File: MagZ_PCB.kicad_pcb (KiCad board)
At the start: 4 copper layers, 42 x 42 mm, 11 parts, among them J6 MTQZ, J8 PQ9-Connector

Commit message: Oops...forgot to save
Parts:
- added G***: LOGO, POQUITO_Panel_Library:POQUITO-7mm, F.Cu at (193.2, 87.2)
- added G***: LOGO, POQUITO_Panel_Library:WSOF-5, F.Cu at (194.6, 70.2)
- added G***: LOGO, POQUITO_Panel_Library:POQUITO-29mm, B.Cu at (193.0, 70.0)
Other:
- board text added: "Designed by Niki Sajjad"
- board text added: "MTQ Z board v1"

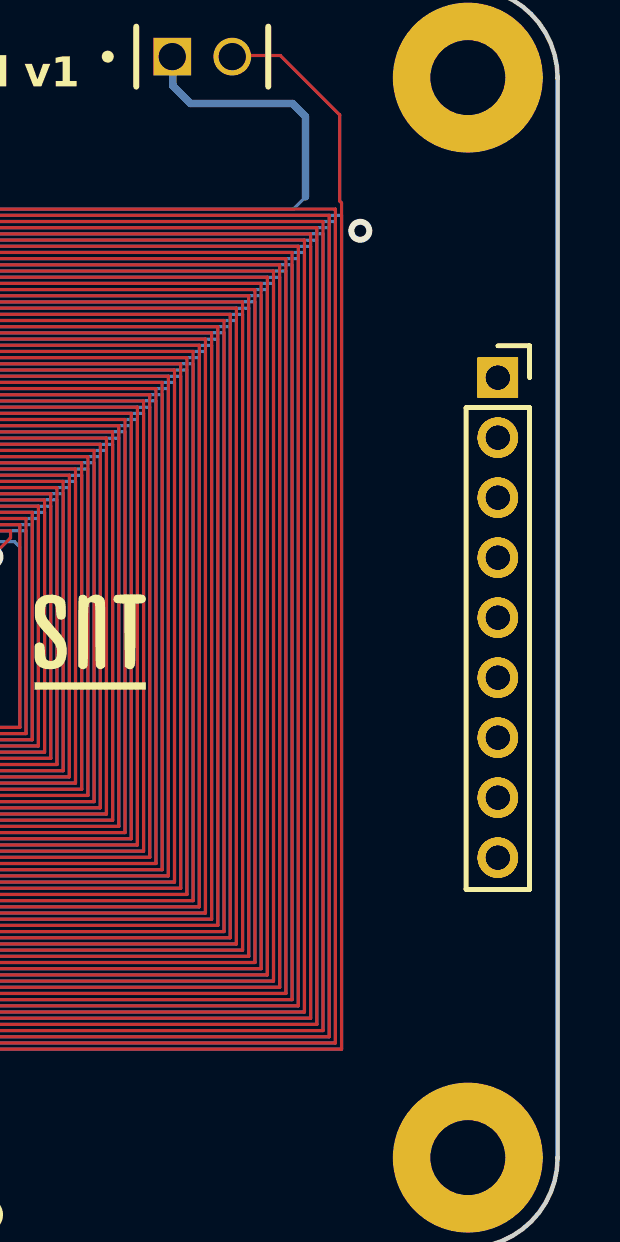
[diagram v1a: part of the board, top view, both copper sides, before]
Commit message: Use pogo pins; move diode to back
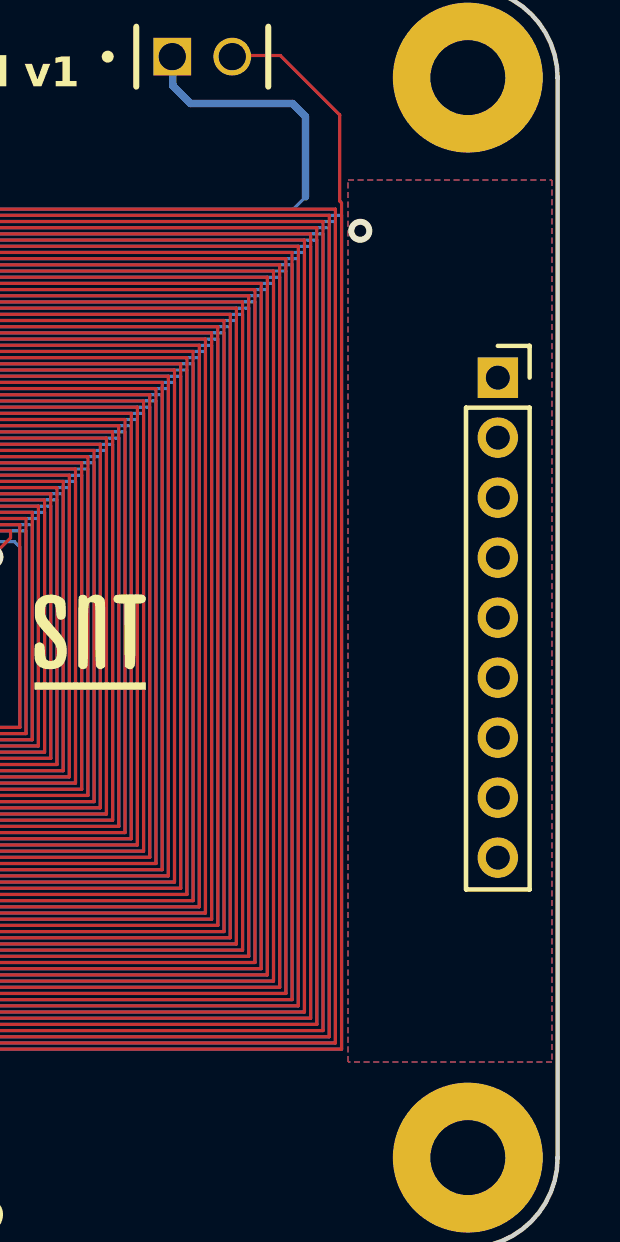
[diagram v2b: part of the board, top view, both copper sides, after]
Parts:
- removed PQ9: PQ9-Connector, Connector_PinSocket_2.00mm:PinSocket_1x09_P2.00mm_Vertical
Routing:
- added copper zone on B.Cu, net GND
- added copper zone on F.Cu, net GND
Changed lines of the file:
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@@
 (kicad_pcb (version 20221018) (generator pcbnew)
   (general
-    (thickness 1.6)
+    (thickness 0.895)
   )
   (paper "A4")
@@
   (net 7 "unconnected-(J8-V3-Pad7)")
   (net 8 "+5V")
-  (net 9 "Net-(PQ9-Pad8)")
-  (net 10 "Net-(PQ9-Pad7)")
-  (net 11 "Net-(PQ9-Pad6)")
-  (net 12 "Net-(PQ9-Pad5)")
-  (net 13 "Net-(PQ9-Pad4)")
-  (net 14 "Net-(PQ9-Pad3)")
-  (net 15 "Net-(PQ9-Pad2)")
-  (net 16 "Net-(PQ9-Pad1)")
   (footprint "Connector_PinSocket_2.00mm:PinSocket_1x09_P2.00mm_Vertical" (layer "F.Cu")
     (at 213.194 61.5879)
@@
       (stroke (width 0) (type solid)) (fill solid) (layer "F.SilkS"))
   )
-  (footprint "Connector_PinSocket_2.00mm:PinSocket_1x09_P2.00mm_Vertical" locked (layer "F.Cu")
-    (at 213.194 61.5879)
-    (descr "Through hole straight socket strip, 1x09, 2.00mm pitch, single row (from Kicad 4.0.7), script generated")
-    (tags "Through hole socket strip THT 1x09 2.00mm single row")
-    (attr through_hole)
-    (fp_text reference "PQ9" (at 0 -2.5 unlocked) (layer "F.SilkS") hide
-        (effects (font (size 0.5 0.5) (thickness 0.1)))
-    )
-    (fp_text value "PQ9-Connector" (at 0 18.5 unlocked) (layer "F.Fab") hide
-        (effects (font (size 0.5 0.5) (thickness 0.1)))
-    )
-    (fp_text user "${REFERENCE}" (at 0 8 90 unlocked) (layer "F.Fab") hide
-        (effects (font (size 0.5 0.5) (thickness 0.1)))
-    )
-    (fp_line (start -1.06 1) (end -1.06 17.06)
-      (stroke (width 0.15) (type solid)) (layer "F.SilkS"))
-    (fp_line (start -1.06 1) (end 1.06 1)
-      (stroke (width 0.15) (type solid)) (layer "F.SilkS"))
-    (fp_line (start -1.06 17.06) (end 1.06 17.06)
-      (stroke (width 0.15) (type solid)) (layer "F.SilkS"))
-    (fp_line (start 0 -1.06) (end 1.06 -1.06)
-      (stroke (width 0.15) (type solid)) (layer "F.SilkS"))
-    (fp_line (start 1.06 -1.06) (end 1.06 0)
-      (stroke (width 0.15) (type solid)) (layer "F.SilkS"))
-    (fp_line (start 1.06 1) (end 1.06 17.06)
-      (stroke (width 0.15) (type solid)) (layer "F.SilkS"))
-    (fp_line (start -1.5 -1.5) (end 1.5 -1.5)
-      (stroke (width 0.05) (type solid)) (layer "F.CrtYd"))
-    (fp_line (start -1.5 17.5) (end -1.5 -1.5)
-      (stroke (width 0.05) (type solid)) (layer "F.CrtYd"))
-    (fp_line (start 1.5 -1.5) (end 1.5 17.5)
-      (stroke (width 0.05) (type solid)) (layer "F.CrtYd"))
-    (fp_line (start 1.5 17.5) (end -1.5 17.5)
-      (stroke (width 0.05) (type solid)) (layer "F.CrtYd"))
-    (fp_line (start -1 -1) (end 0.5 -1)
-      (stroke (width 0.1) (type solid)) (layer "F.Fab"))
-    (fp_line (start -1 17) (end -1 -1)
-      (stroke (width 0.1) (type solid)) (layer "F.Fab"))
-    (fp_line (start 0.5 -1) (end 1 -0.5)
-      (stroke (width 0.1) (type solid)) (layer "F.Fab"))
-    (fp_line (start 1 -0.5) (end 1 17)
-      (stroke (width 0.1) (type solid)) (layer "F.Fab"))
-    (fp_line (start 1 17) (end -1 17)
-      (stroke (width 0.1) (type solid)) (layer "F.Fab"))
-    (pad "1" thru_hole rect locked (at 0 0) (size 1.35 1.35) (drill 0.8) (layers "*.Cu" "*.Mask")
-      (net 16 "Net-(PQ9-Pad1)"))
-    (pad "2" thru_hole oval locked (at 0 2) (size 1.35 1.35) (drill 0.8) (layers "*.Cu" "*.Mask")
-      (net 15 "Net-(PQ9-Pad2)"))
-    (pad "3" thru_hole oval locked (at 0 4) (size 1.35 1.35) (drill 0.8) (layers "*.Cu" "*.Mask")
-      (net 14 "Net-(PQ9-Pad3)"))
-    (pad "4" thru_hole oval locked (at 0 6) (size 1.35 1.35) (drill 0.8) (layers "*.Cu" "*.Mask")
-      (net 13 "Net-(PQ9-Pad4)"))
-    (pad "5" thru_hole oval locked (at 0 8) (size 1.35 1.35) (drill 0.8) (layers "*.Cu" "*.Mask")
-      (net 12 "Net-(PQ9-Pad5)"))
-    (pad "6" thru_hole oval locked (at 0 10) (size 1.35 1.35) (drill 0.8) (layers "*.Cu" "*.Mask")
-      (net 11 "Net-(PQ9-Pad6)"))
-    (pad "7" thru_hole oval locked (at 0 12) (size 1.35 1.35) (drill 0.8) (layers "*.Cu" "*.Mask")
-      (net 10 "Net-(PQ9-Pad7)"))
-    (pad "8" thru_hole oval locked (at 0 14) (size 1.35 1.35) (drill 0.8) (layers "*.Cu" "*.Mask")
-      (net 9 "Net-(PQ9-Pad8)"))
-    (pad "9" thru_hole oval locked (at 0 16) (size 1.35 1.35) (drill 0.8) (layers "*.Cu" "*.Mask")
-      (net 13 "Net-(PQ9-Pad4)"))
-    (model "${KISYS3DMOD}/Connector_PinSocket_2.00mm.3dshapes/PinSocket_1x09_P2.00mm_Vertical.wrl"
-      (offset (xyz 0 0 0))
-      (scale (xyz 1 1 1))
-      (rotate (xyz 0 0 0))
-    )
-  )
   (footprint "MountingHole:MountingHole_2.5mm_Pad" locked (layer "F.Cu")
     (at 176.194 51.5879)
@@
   (segment (start 183.6981 59.6835) (end 183.6981 80.2587) (width 0.1062) (layer "B.Cu") (net 0))
   (segment (start 184.5231 60.5085) (end 184.5231 79.4337) (width 0.1062) (layer "B.Cu") (net 0))
+  (zone (net 1) (net_name "GND") (layer "F.Cu") (hatch edge 0.5)
+    (connect_pads (clearance 0.5))
+    (min_thickness 0.25) (filled_areas_thickness no)
+    (fill yes (thermal_gap 0.5) (thermal_bridge_width 0.5))
+    (polygon
+      (pts
+        (xy 215 55)
+        (xy 215 84.4)
+        (xy 208.2 84.4)
+        (xy 208.2 55)
+      )
+    )
+  )
+  (zone (net 1) (net_name "GND") (layer "B.Cu") (hatch edge 0.5)
+    (connect_pads (clearance 0.5))
+    (min_thickness 0.25) (filled_areas_thickness no)
+    (fill yes (thermal_gap 0.5) (thermal_bridge_width 0.5))
+    (polygon
+      (pts
+        (xy 215 55)
+        (xy 215 84.4)
+        (xy 208.2 84.4)
+        (xy 208.2 55)
+      )
+    )
+  )
 )

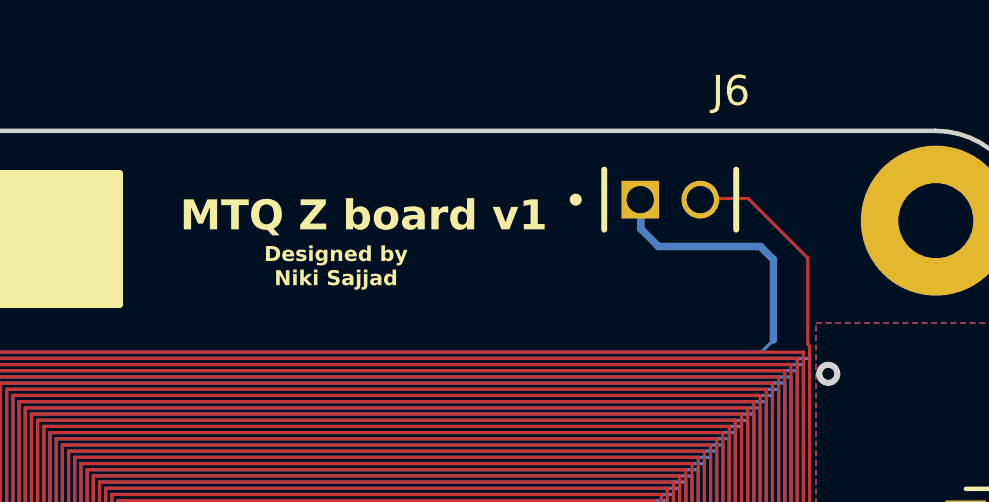
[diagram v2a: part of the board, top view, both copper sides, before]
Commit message: Flip misaligned pogo pins
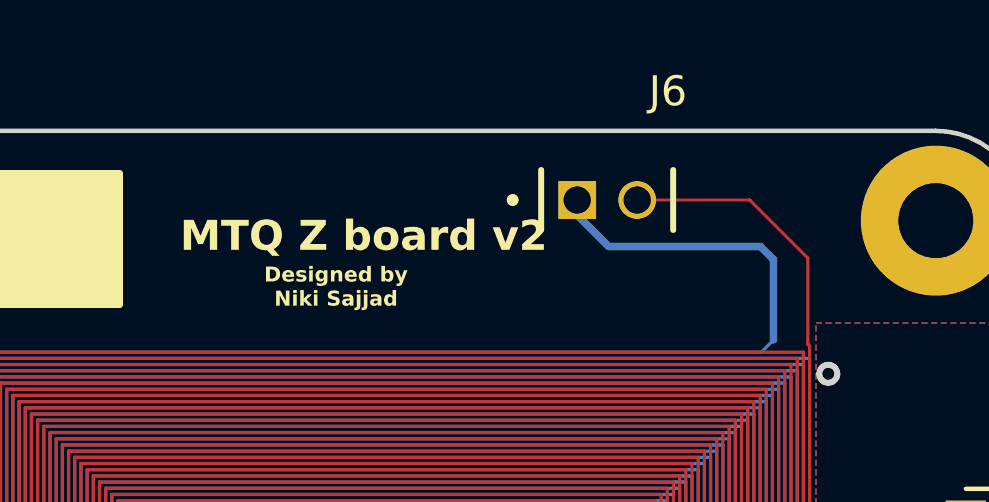
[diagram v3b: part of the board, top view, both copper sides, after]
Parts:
- moved J6 2.10 mm to (200.2, 50.9)
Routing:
- net (no net): track 14674.0 -> 14677.9 mm
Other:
- board text added: "MTQ Z board v2"
- board text removed: "MTQ Z board v1"

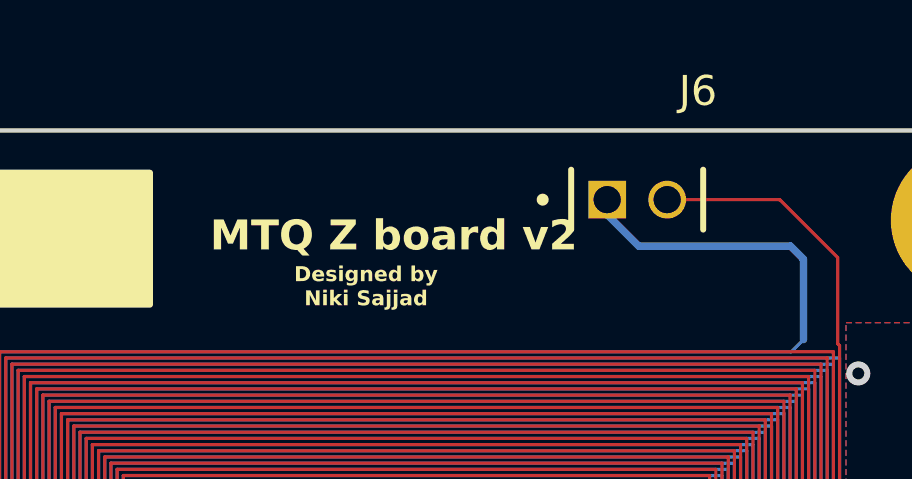
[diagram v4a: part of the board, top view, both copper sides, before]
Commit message: Fix PTH mounting holes for MTQ
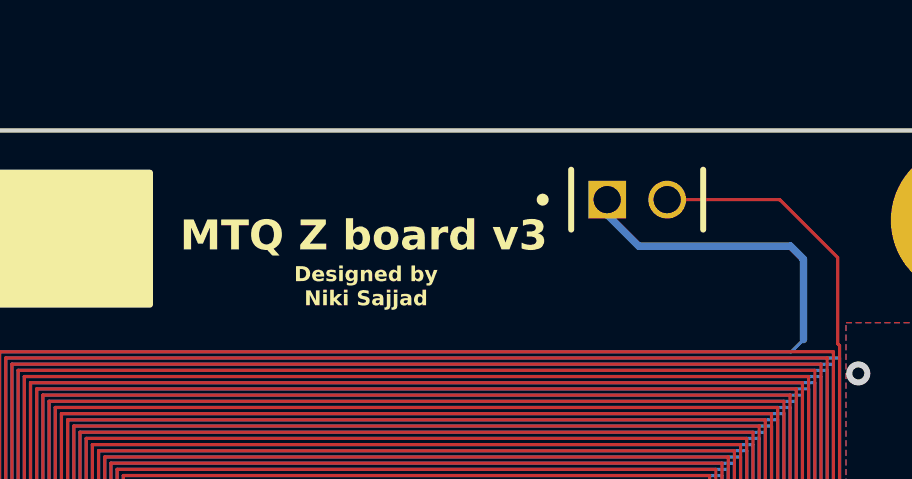
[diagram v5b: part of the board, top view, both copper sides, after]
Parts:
- removed REF** (x4): MountingHole_2.5mm_Pad, MountingHole:MountingHole_2.5mm_Pad
- added ?: , , F.Cu at (212.2, 87.6)
- added ?: , , F.Cu at (212.2, 51.6)
- added ?: , , F.Cu at (176.2, 87.6)
- added ?: , , F.Cu at (176.2, 51.6)
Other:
- board text added: "MTQ Z board v3"
- board text removed: "MTQ Z board v2"
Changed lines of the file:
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@@
       (solder_mask_margin 0.5) (clearance 0.5))
   )
+  (footprint "" (layer "F.Cu")
+    (at 212.194 87.5879)
+    (fp_text reference "" (at 0 0) (layer "F.SilkS")
+        (effects (font (size 1.27 1.27) (thickness 0.15)))
+    )
+    (fp_text value "" (at 0 0) (layer "F.SilkS")
+        (effects (font (size 1.27 1.27) (thickness 0.15)))
+    )
+    (pad "1" thru_hole circle (at 0 0) (size 5 5) (drill 2.5) (layers "*.Cu" "*.Mask")
+      (pinfunction "1") (pintype "input+no_connect"))
+  )
   (footprint "Fiducial:Fiducial_0.5mm_Mask1.5mm" (layer "F.Cu")
     (at 98.2428 120.958)
@@
     (property "SnapEDA_Link" "https://www.snapeda.com/parts/SQT-102-03-F-S/Samtec/view-part/?ref=snap")
     (attr through_hole)
-    (fp_text reference "J6" (at 3.025 -3.62) (layer "F.SilkS")
+    (fp_text reference "J6" (at 3.025 -3.62) (layer "F.SilkS") hide
         (effects (font (size 1 1) (thickness 0.15)))
     )
@@
       (pinfunction "02") (pintype "passive") (solder_mask_margin 0.102))
   )
+  (footprint "" (layer "F.Cu")
+    (at 212.194 51.5879)
+    (fp_text reference "" (at 0 0) (layer "F.SilkS")
+        (effects (font (size 1.27 1.27) (thickness 0.15)))
+    )
+    (fp_text value "" (at 0 0) (layer "F.SilkS")
+        (effects (font (size 1.27 1.27) (thickness 0.15)))
+    )
+    (pad "1" thru_hole circle (at 0 0) (size 5 5) (drill 2.5) (layers "*.Cu" "*.Mask")
+      (pinfunction "1") (pintype "input+no_connect"))
+  )
   (footprint "POQUITO_Panel_Library:POQUITO-7mm" (layer "F.Cu")
     (at 193.2 87.2)
@@
       (stroke (width 0) (type solid)) (fill solid) (layer "F.SilkS"))
   )
-  (footprint "MountingHole:MountingHole_2.5mm_Pad" locked (layer "F.Cu")
-    (at 176.194 51.5879)
-    (descr "Mounting Hole 2.5mm")
-    (tags "mounting hole 2.5mm")
-    (zone_connect 0)
-    (attr exclude_from_pos_files exclude_from_bom)
-    (fp_text reference "REF**" (at 0 -3.5 unlocked) (layer "F.SilkS") hide
-        (effects (font (size 0.5 0.5) (thickness 0.1)))
-    )
-    (fp_text value "MountingHole_2.5mm_Pad" (at -13 0 unlocked) (layer "F.Fab") hide
-        (effects (font (size 0.5 0.5) (thickness 0.1)))
-    )
-    (fp_text user "${REFERENCE}" (at 0.3 0 unlocked) (layer "F.Fab")
-        (effects (font (size 0.5 0.5) (thickness 0.1)))
-    )
-    (fp_circle (center 0 0) (end 2.5 0)
-      (stroke (width 0.15) (type solid)) (fill none) (layer "Cmts.User"))
-    (fp_circle (center 0 0) (end 2.75 0)
-      (stroke (width 0.05) (type solid)) (fill none) (layer "F.CrtYd"))
-    (pad "" np_thru_hole circle locked (at 0 0) (size 5 5) (drill 2.5) (layers "*.Cu" "*.Mask")
-      (zone_connect 0))
-  )
-  (footprint "MountingHole:MountingHole_2.5mm_Pad" locked (layer "F.Cu")
-    (at 176.194 87.5879)
-    (descr "Mounting Hole 2.5mm")
-    (tags "mounting hole 2.5mm")
-    (attr exclude_from_pos_files exclude_from_bom)
-    (fp_text reference "REF**" (at 0 -3.5 unlocked) (layer "F.SilkS") hide
-        (effects (font (size 0.5 0.5) (thickness 0.1)))
-    )
-    (fp_text value "MountingHole_2.5mm_Pad" (at -13 0 unlocked) (layer "F.Fab") hide
-        (effects (font (size 0.5 0.5) (thickness 0.1)))
-    )
-    (fp_text user "${REFERENCE}" (at 0.3 0 unlocked) (layer "F.Fab")
-        (effects (font (size 0.5 0.5) (thickness 0.1)))
-    )
-    (fp_circle (center 0 0) (end 2.5 0)
-      (stroke (width 0.15) (type solid)) (fill none) (layer "Cmts.User"))
-    (fp_circle (center 0 0) (end 2.75 0)
-      (stroke (width 0.05) (type solid)) (fill none) (layer "F.CrtYd"))
-    (pad "" np_thru_hole circle locked (at 0 0) (size 5 5) (drill 2.5) (layers "*.Cu" "*.Mask"))
-  )
-  (footprint "MountingHole:MountingHole_2.5mm_Pad" locked (layer "F.Cu")
-    (at 212.194 87.5879)
-    (descr "Mounting Hole 2.5mm")
-    (tags "mounting hole 2.5mm")
-    (attr exclude_from_pos_files exclude_from_bom)
-    (fp_text reference "REF**" (at 0 -3.5 unlocked) (layer "F.SilkS") hide
-        (effects (font (size 0.5 0.5) (thickness 0.1)))
-    )
-    (fp_text value "MountingHole_2.5mm_Pad" (at 13 0 unlocked) (layer "F.Fab") hide
-        (effects (font (size 0.5 0.5) (thickness 0.1)))
-    )
-    (fp_text user "${REFERENCE}" (at 0.3 0 unlocked) (layer "F.Fab")
-        (effects (font (size 0.5 0.5) (thickness 0.1)))
-    )
-    (fp_circle (center 0 0) (end 2.5 0)
-      (stroke (width 0.15) (type solid)) (fill none) (layer "Cmts.User"))
-    (fp_circle (center 0 0) (end 2.75 0)
-      (stroke (width 0.05) (type solid)) (fill none) (layer "F.CrtYd"))
-    (pad "" np_thru_hole circle locked (at 0 0) (size 5 5) (drill 2.5) (layers "*.Cu" "*.Mask"))
-  )
   (footprint "POQUITO_Panel_Library:WSOF-5" (layer "F.Cu")
     (at 194.570376 70.225606)
@@
       (stroke (width 0) (type solid)) (fill solid) (layer "F.SilkS"))
   )
-  (footprint "MountingHole:MountingHole_2.5mm_Pad" locked (layer "F.Cu")
-    (at 212.194 51.5879)
-    (descr "Mounting Hole 2.5mm")
-    (tags "mounting hole 2.5mm")
-    (attr exclude_from_pos_files exclude_from_bom)
-    (fp_text reference "REF**" (at 0 -3.5 unlocked) (layer "F.SilkS") hide
-        (effects (font (size 0.5 0.5) (thickness 0.1)))
+  (footprint "" (layer "F.Cu")
+    (at 176.194 87.5879)
+    (fp_text reference "" (at 0 0) (layer "F.SilkS")
+        (effects (font (size 1.27 1.27) (thickness 0.15)))
     )
-    (fp_text value "MountingHole_2.5mm_Pad" (at 13 0 unlocked) (layer "F.Fab") hide
-        (effects (font (size 0.5 0.5) (thickness 0.1)))
+    (fp_text value "" (at 0 0) (layer "F.SilkS")
+        (effects (font (size 1.27 1.27) (thickness 0.15)))
     )
-    (fp_text user "${REFERENCE}" (at 0.3 0 unlocked) (layer "F.Fab")
-        (effects (font (size 0.5 0.5) (thickness 0.1)))
+    (pad "1" thru_hole circle (at 0 0) (size 5 5) (drill 2.5) (layers "*.Cu" "*.Mask")
+      (pinfunction "1") (pintype "input+no_connect"))
+  )
+  (footprint "" (layer "F.Cu")
+    (at 176.194 51.5879)
+    (fp_text reference "" (at 0 0) (layer "F.SilkS")
+        (effects (font (size 1.27 1.27) (thickness 0.15)))
     )
-    (fp_circle (center 0 0) (end 2.5 0)
-      (stroke (width 0.15) (type solid)) (fill none) (layer "Cmts.User"))
-    (fp_circle (center 0 0) (end 2.75 0)
-      (stroke (width 0.05) (type solid)) (fill none) (layer "F.CrtYd"))
-    (pad "" np_thru_hole circle locked (at 0 0) (size 5 5) (drill 2.5) (layers "*.Cu" "*.Mask"))
+    (fp_text value "" (at 0 0) (layer "F.SilkS")
+        (effects (font (size 1.27 1.27) (thickness 0.15)))
+    )
+    (pad "1" thru_hole circle (at 0 0) (size 5 5) (drill 2.5) (layers "*.Cu" "*.Mask")
+      (pinfunction "1") (pintype "input+no_connect"))
   )
   (footprint "POQUITO_Panel_Library:POQUITO-29mm" (layer "B.Cu")
@@
     (effects (font (size 0.5 0.5) (thickness 0.1) bold) (justify bottom))
   )
-  (gr_text "MTQ Z board v2" (at 187 52.683) (layer "F.SilkS")
+  (gr_text "MTQ Z board v3" (at 186 52.683) (layer "F.SilkS")
     (effects (font (size 1 1) (thickness 0.2) bold) (justify left bottom))
   )
